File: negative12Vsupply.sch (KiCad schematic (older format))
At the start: 20 parts, among them U2 LT3959

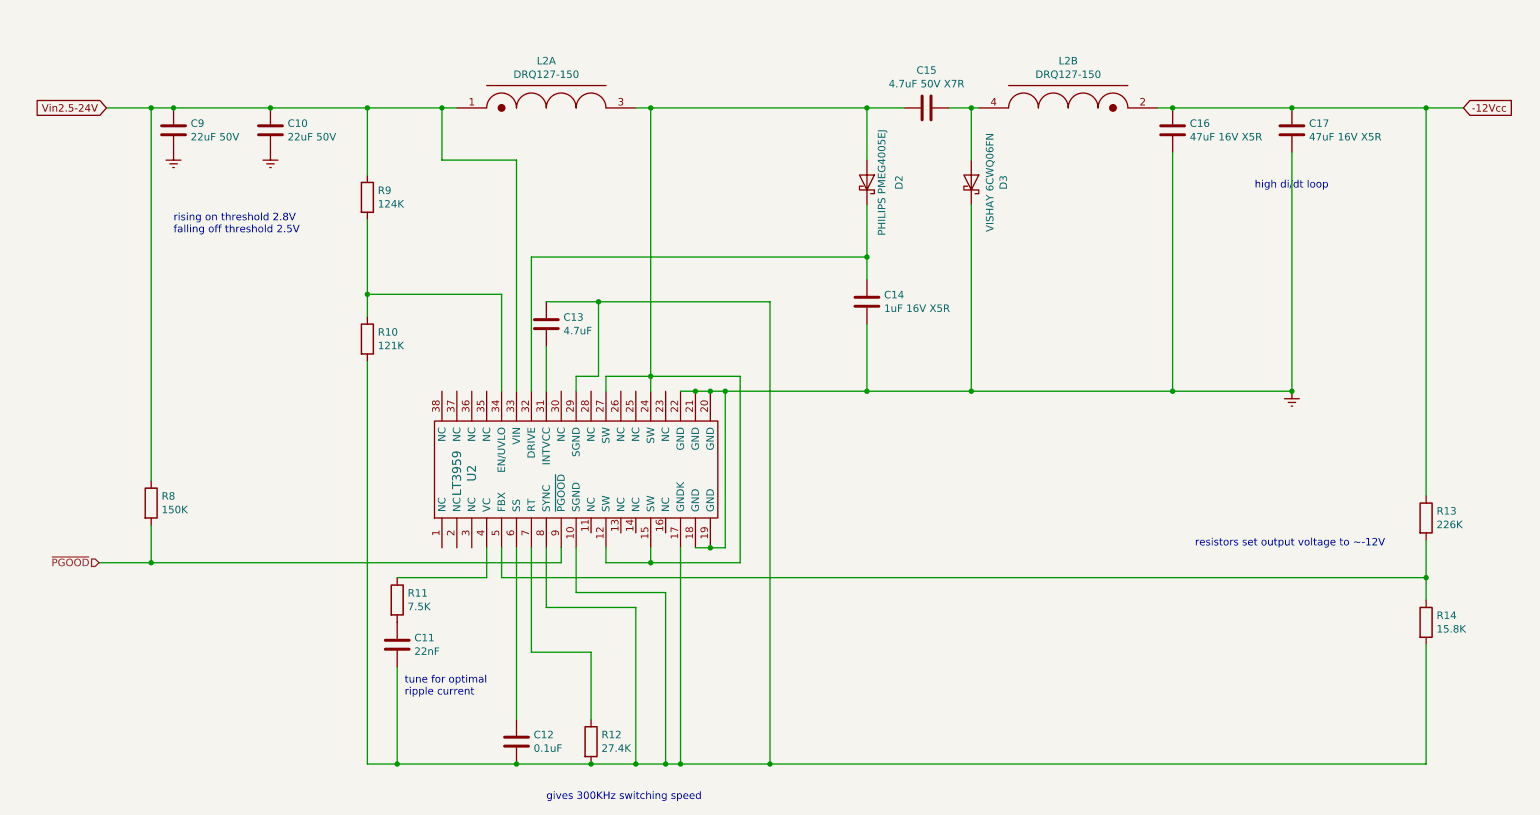
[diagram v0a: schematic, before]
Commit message: Named nets, made it use 2 inductors
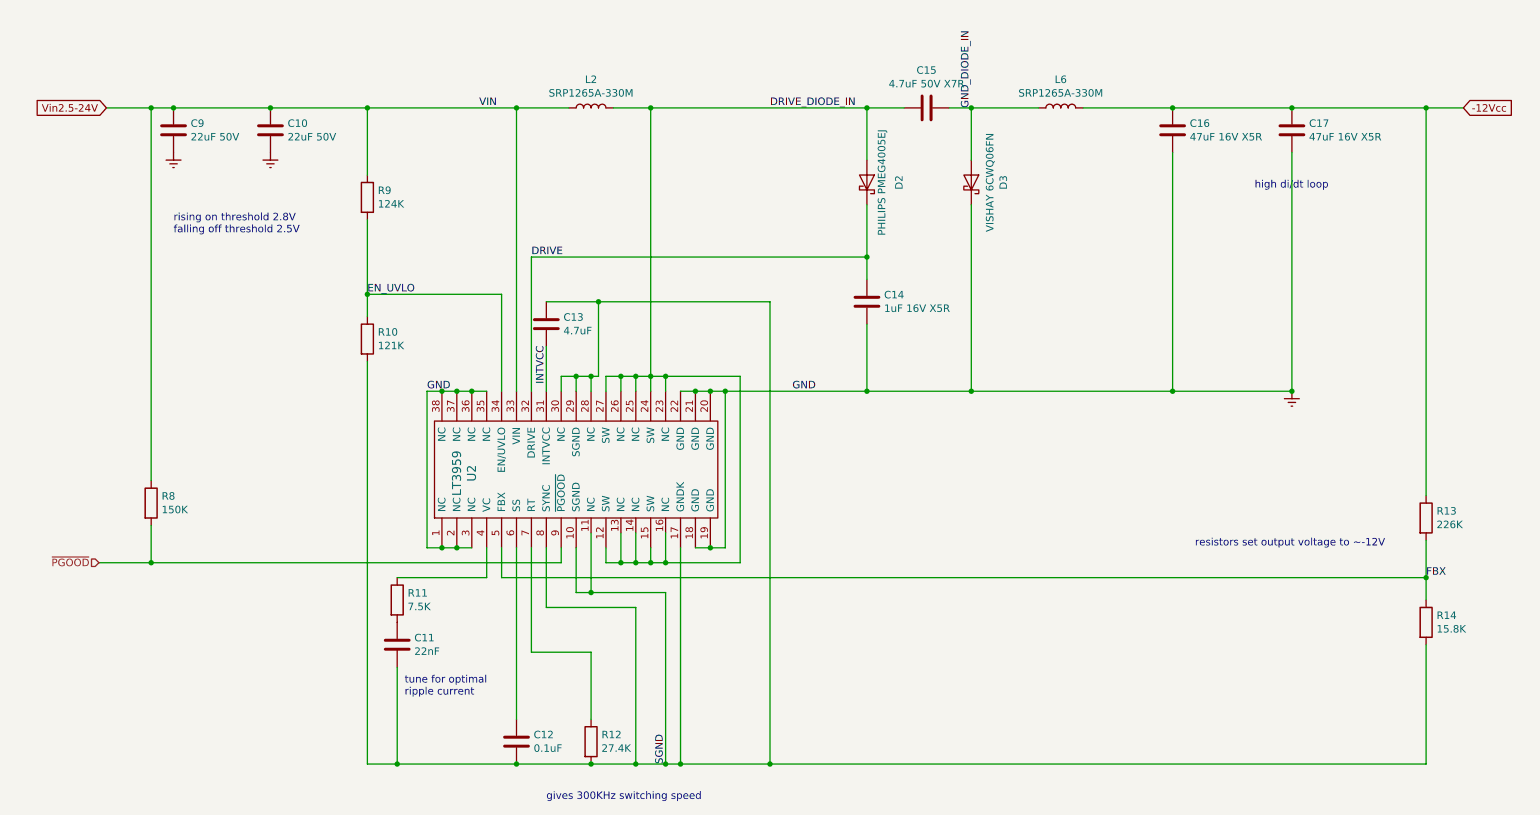
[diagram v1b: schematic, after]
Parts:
- removed L2: DRQ127-150, eaton:eaton_drq127, symbol coiltronics:DRQ127-150
- added L2, L6: SRP1265A-330M, bourns:bourns_srp1265a, symbol Device:L
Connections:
- net -12Vcc: now also L6.2
- net Earth: now also U2.1 (NC), U2.2 (NC), U2.3 (NC), U2.35 (NC), U2.36 (NC), U2.37 (NC), U2.38 (NC)
- net Vin2.5-24V: now also L2.1
- net SGND: now reaches C11.2, C12.2, C13.1, R10.2, R12.2, R14.2, U2.10 (SGND), U2.17 (GNDK), U2.29 (SGND), U2.8 (SYNC)
- net SGND: now also U2.11 (NC), U2.28 (NC), U2.30 (NC)
- net INTVCC: now reaches C13.2, U2.31 (INTVCC)
- net GND_DIODE_IN: now reaches C15.2, D3.2 (A)
- net GND_DIODE_IN: now also L6.1
- net DRIVE_DIODE_IN: now reaches C15.1, D2.2 (A), U2.12 (SW), U2.15 (SW), U2.24 (SW), U2.27 (SW)
- net DRIVE_DIODE_IN: now also U2.13 (NC), U2.14 (NC), U2.16 (NC), U2.23 (NC), U2.25 (NC), U2.26 (NC), L2.2
- net DRIVE: now reaches C14.1, D2.1 (K), U2.32 (DRIVE)
- net EN_UVLO: now reaches R10.1, R9.2, U2.34 (EN/UVLO)
- net FBX: now reaches R13.2, R14.1, U2.5 (FBX)
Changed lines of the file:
@@
 	5400 4600 5400 5750
 Wire Wire Line
-	4800 4600 5400 4600
+	4800 4600 4900 4600
 Wire Wire Line
 	4800 4300 4800 4600
@@
 	5500 4300 5500 5750
 Wire Wire Line
-	5300 4400 5000 4400
+	5300 4400 5200 4400
 Wire Wire Line
 	5300 4300 5300 4400
@@
 Connection ~ 5300 4400
 Wire Wire Line
-	5900 4400 5300 4400
+	5900 4400 5400 4400
 Connection ~ 3600 5750
 Wire Wire Line
@@
 Wire Wire Line
 	9600 1650 9600 3250
-$Comp
-L coiltronics:DRQ127-150 L?
-U 2 1 5CA63937
-P 8100 1100
-AR Path="/5CA63937" Ref="L?"  Part="2"
-AR Path="/5CA65B33/5CA63937" Ref="L?"  Part="2"
-AR Path="/5CA63886/5CA63937" Ref="L2"  Part="2"
-F 0 "L2" H 8100 1165 50  0000 C CNN
-F 1 "DRQ127-150" H 8100 1074 50  0000 C CNN
-F 2 "eaton:eaton_drq127" H 8100 1100 50  0001 C CNN
-F 3 "" H 8100 1100 50  0001 C CNN
-	2    8100 1100
-	1    0    0    -1
-$EndComp
-Wire Wire Line
-	4400 1700 4400 3250
-Wire Wire Line
-	3900 1700 4400 1700
-Wire Wire Line
-	3900 1350 3900 1700
-$Comp
-L coiltronics:DRQ127-150 L?
-U 1 1 5CA63936
-P 4600 1100
-AR Path="/5CA63936" Ref="L?"  Part="1"
-AR Path="/5CA65B33/5CA63936" Ref="L?"  Part="1"
-AR Path="/5CA63886/5CA63936" Ref="L2"  Part="1"
-F 0 "L2" H 4600 1165 50  0000 C CNN
-F 1 "DRQ127-150" H 4600 1074 50  0000 C CNN
-F 2 "eaton:eaton_drq127" H 4600 1100 50  0001 C CNN
-F 3 "" H 4600 1100 50  0001 C CNN
-	1    4600 1100
-	-1   0    0    -1
-$EndComp
 Text Notes 9350 1900 0    50   ~ 0
 high di/dt loop
@@
 	4950 3150 4950 2650
 Wire Wire Line
-	4800 3150 4950 3150
+	4800 3150 4900 3150
 Wire Wire Line
 	4800 3250 4800 3150
@@
 	5900 3150 5900 4400
 Wire Wire Line
-	5300 3150 5900 3150
+	5300 3150 5400 3150
 Wire Wire Line
 	5300 3150 5300 3250
@@
 	5000 3150 5000 3250
 Wire Wire Line
-	5000 3150 5300 3150
+	5000 3150 5100 3150
 Wire Wire Line
 	1950 3850 1950 1350
@@
 Wire Wire Line
 	7450 3250 8800 3250
-Wire Wire Line
-	7450 1350 7500 1350
-Wire Wire Line
-	8700 1350 8800 1350
 Connection ~ 8800 1350
 $Comp
@@
 	5300 1350 5300 3150
 Wire Wire Line
-	5200 1350 5300 1350
-Wire Wire Line
 	5300 1350 6750 1350
 Connection ~ 5300 1350
 Wire Wire Line
-	4000 1350 3900 1350
-Connection ~ 3900 1350
-Wire Wire Line
 	2750 1350 3400 1350
 Wire Wire Line
@@
 Connection ~ 3400 1350
 Wire Wire Line
-	3400 1350 3900 1350
-Wire Wire Line
 	3400 2100 3400 2600
 Connection ~ 3400 2600
+$Comp
+L Device:L L2
+U 1 1 5CB62A4C
+P 4900 1350
+F 0 "L2" V 5090 1350 50  0000 C CNN
+F 1 "SRP1265A-330M" V 4999 1350 50  0000 C CNN
+F 2 "bourns:bourns_srp1265a" H 4900 1350 50  0001 C CNN
+F 3 "~" H 4900 1350 50  0001 C CNN
+	1    4900 1350
+	0    -1   -1   0
+$EndComp
+Wire Wire Line
+	5050 1350 5300 1350
+Connection ~ 4400 1350
+Wire Wire Line
+	4400 1350 4750 1350
+Wire Wire Line
+	4400 1350 4400 3250
+Wire Wire Line
+	3400 1350 4400 1350
+$Comp
+L Device:L L6
+U 1 1 5CB70FAA
+P 8050 1350
+F 0 "L6" V 8240 1350 50  0000 C CNN
+F 1 "SRP1265A-330M" V 8149 1350 50  0000 C CNN
+F 2 "bourns:bourns_srp1265a" H 8050 1350 50  0001 C CNN
+F 3 "~" H 8050 1350 50  0001 C CNN
+	1    8050 1350
+	0    -1   -1   0
+$EndComp
+Wire Wire Line
+	7450 1350 7900 1350
+Wire Wire Line
+	8200 1350 8800 1350
+Text Label 4500 2350 0    50   ~ 0
+DRIVE
+Text Label 6100 1350 0    50   ~ 0
+DRIVE_DIODE_IN
+Text Label 6250 3250 0    50   ~ 0
+GND
+Text Label 7450 1350 1    50   ~ 0
+GND_DIODE_IN
+Text Label 5400 5750 1    50   ~ 0
+SGND
+Text Label 3400 2600 0    50   ~ 0
+EN_UVLO
+Text Label 4150 1350 0    50   ~ 0
+VIN
+Text Label 4600 3200 1    50   ~ 0
+INTVCC
+Wire Wire Line
+	4900 3250 4900 3150
+Connection ~ 4900 3150
+Wire Wire Line
+	4900 3150 4950 3150
+Wire Wire Line
+	4900 4200 4900 4600
+Connection ~ 4900 4600
+Wire Wire Line
+	4900 4600 5400 4600
+Wire Wire Line
+	5100 4200 5100 4400
+Connection ~ 5100 4400
+Wire Wire Line
+	5100 4400 5000 4400
+Wire Wire Line
+	5200 4200 5200 4400
+Connection ~ 5200 4400
+Wire Wire Line
+	5200 4400 5100 4400
+Wire Wire Line
+	5400 4200 5400 4400
+Connection ~ 5400 4400
+Wire Wire Line
+	5400 4400 5300 4400
+Wire Wire Line
+	5400 3250 5400 3150
+Connection ~ 5400 3150
+Wire Wire Line
+	5400 3150 5900 3150
+Wire Wire Line
+	5200 3250 5200 3150
+Connection ~ 5200 3150
+Wire Wire Line
+	5200 3150 5300 3150
+Wire Wire Line
+	5100 3250 5100 3150
+Connection ~ 5100 3150
+Wire Wire Line
+	5100 3150 5200 3150
+Wire Wire Line
+	4100 4300 4000 4300
+Wire Wire Line
+	4000 4300 3900 4300
+Connection ~ 4000 4300
+Wire Wire Line
+	3900 3250 4000 3250
+Wire Wire Line
+	4000 3250 4100 3250
+Connection ~ 4000 3250
+Wire Wire Line
+	4100 3250 4200 3250
+Connection ~ 4100 3250
+Wire Wire Line
+	3900 3250 3800 3250
+Wire Wire Line
+	3800 3250 3800 4300
+Wire Wire Line
+	3800 4300 3900 4300
+Connection ~ 3900 3250
+Connection ~ 3900 4300
+Text Label 3800 3250 0    50   ~ 0
+GND
+Wire Wire Line
+	4700 3250 4700 3150
+Wire Wire Line
+	4700 3150 4800 3150
+Connection ~ 4800 3150
+Text Label 10500 4500 0    50   ~ 0
+FBX
 $EndSCHEMATC

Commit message: Use better footprint for TO-252 diode package
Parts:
- D3: footprint Package_TO_SOT_SMD:TO-252-2 -> generic:D_TO-252
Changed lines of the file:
@@
 F 0 "D3" H 7450 2066 50  0000 C CNN
 F 1 "VISHAY 6CWQ06FN" H 7450 1975 50  0000 C CNN
-F 2 "Package_TO_SOT_SMD:TO-252-2" H 7450 1850 50  0001 C CNN
+F 2 "generic:D_TO-252" H 7450 1850 50  0001 C CNN
 F 3 "~" H 7450 1850 50  0001 C CNN
 	1    7450 1850
